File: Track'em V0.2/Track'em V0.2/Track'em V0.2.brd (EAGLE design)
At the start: 47.2 x 17 mm, 36 parts, among them IC1 SAM-M8Q, J1 CORTEX_DEBUG_PTH, U2 3.3V/150mA, Y1 26MHz

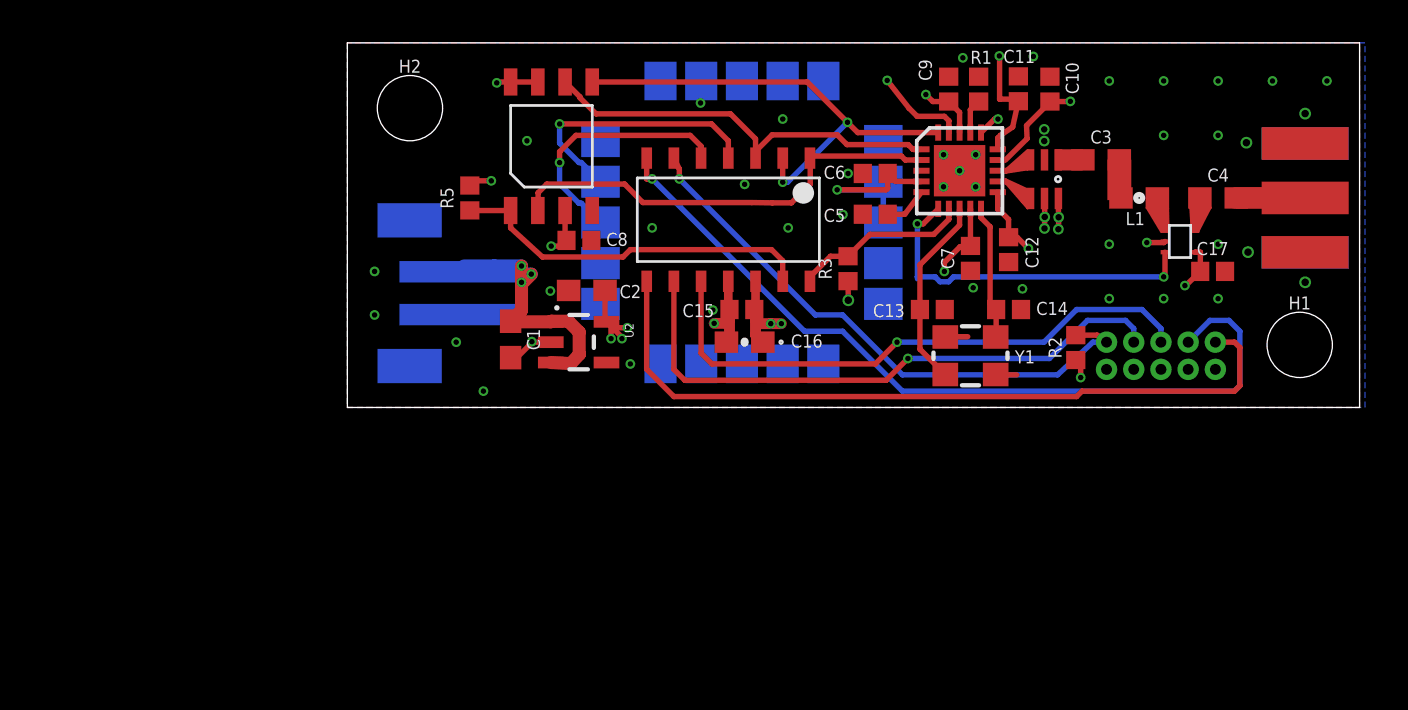
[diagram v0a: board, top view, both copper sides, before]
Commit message: tracking message parsed from GPS
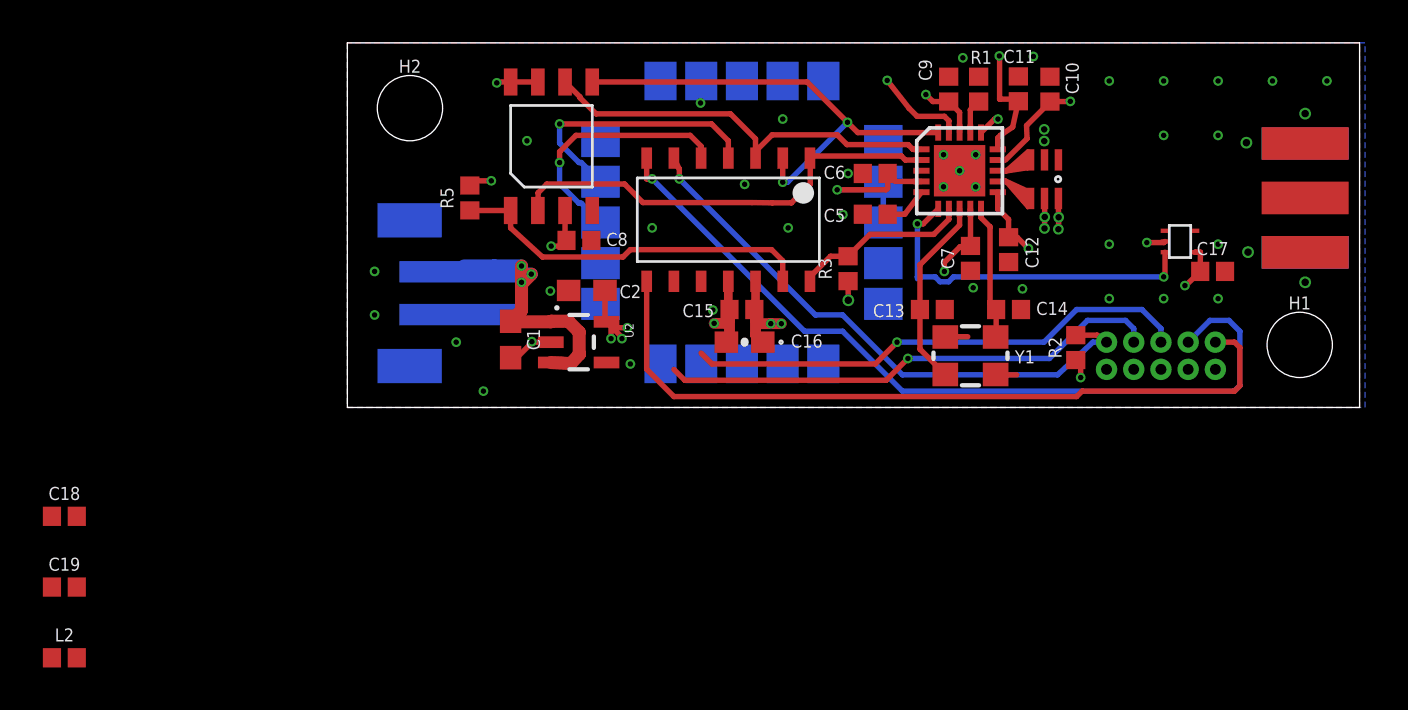
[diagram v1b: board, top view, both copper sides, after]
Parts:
- removed C3, C4: 1000pF, SparkFun-Capacitors:0603
- removed L1: 6.8nH, SparkFun-Passives:0603
- added C18, C19: 1000pF, SparkFun-Capacitors:0402
- added L2: 6.8NH, SparkFun-Coils:0402
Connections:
- net N$1: now also L2.2; no longer L1.2
- net N$13: now also C19.2; no longer C4.2
- net N$2: now also C18.2, L2.1; no longer C3.2, L1.1
- net N$3: now also C19.1; no longer C4.1
- net UBAL: now also C18.1; no longer C3.1
- net USART_RX: now also U$2.9; no longer U$2.10
- net USART_TX: now also U$2.10; no longer U$2.9
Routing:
- net N$1: track 10.5 -> 0.00 mm
- net N$3: track 9.14 -> 0.00 mm
- net USART_TX: track 27.7 -> 23.6 mm
- net USART_RX: track 27.1 -> 23.7 mm
- net N$13: track 3.21 -> 0.00 mm
- net N$2: track 1.81 -> 0.00 mm
- net UBAL: track 1.15 -> 0.00 mm
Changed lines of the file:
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@@
 <wire x1="47.244" y1="17.018" x2="0" y2="17.018" width="0" layer="20"/>
 <wire x1="0" y1="17.018" x2="0" y2="0" width="0" layer="20"/>
-<rectangle x1="33.0073" y1="11.0617" x2="34.3281" y2="12.0523" layer="1"/>
-<rectangle x1="35.4711" y1="9.6774" x2="36.5887" y2="11.5697" layer="1"/>
 <rectangle x1="33.02" y1="11.049" x2="36.7538" y2="12.0396" layer="39"/>
 <polygon width="0.508" layer="41">
@@
 <element name="J$1" library="SparkFun-Connectors" package="SMA-EDGE" value="SMA_EDGE" x="44.704" y="12.319" rot="R270"/>
 <element name="U$4" library="SaL-lib1" package="AN26018A" value="AN26018A" x="38.862" y="7.747" rot="R270"/>
-<element name="C3" library="SparkFun-Capacitors" package="0603" value="1000pF" x="35.179" y="11.557" smashed="yes">
-<attribute name="NAME" x="35.179" y="12.319" size="0.6096" layer="25" font="vector" ratio="20" align="bottom-center"/>
-<attribute name="PROD_ID" value="CAP-07888" x="35.179" y="11.557" size="1.778" layer="27" display="off"/>
-</element>
-<element name="L1" library="SparkFun-Passives" package="0603" value="6.8nH" x="36.957" y="9.779" smashed="yes">
-<attribute name="NAME" x="36.322" y="8.509" size="0.6096" layer="25" font="vector" ratio="20"/>
-</element>
-<element name="C4" library="SparkFun-Capacitors" package="0603" value="1000pF" x="40.64" y="9.779" smashed="yes">
-<attribute name="NAME" x="40.64" y="10.541" size="0.6096" layer="25" font="vector" ratio="20" align="bottom-center"/>
-<attribute name="PROD_ID" value="CAP-07888" x="40.64" y="9.779" size="1.778" layer="27" display="off"/>
-</element>
 <element name="H1" library="SparkFun-Hardware" package="STAND-OFF-TIGHT" value="STAND-OFFTIGHT" x="44.45" y="2.921" smashed="yes">
 <attribute name="NAME" x="44.45" y="4.572" size="0.6096" layer="25" font="vector" ratio="20" align="bottom-center"/>
@@
 <element name="C17" library="SparkFun-Capacitors" package="0402" value="0.1uF" x="40.386" y="6.35">
 <attribute name="PROD_ID" value="CAP-12416" x="40.386" y="6.35" size="1.778" layer="27" display="off"/>
+</element>
+<element name="C18" library="SparkFun-Capacitors" package="0402" value="1000pF" x="-13.208" y="-5.08">
+<attribute name="PROD_ID" value="CAP-12416" x="-13.208" y="-5.08" size="1.778" layer="27" display="off"/>
+</element>
+<element name="C19" library="SparkFun-Capacitors" package="0402" value="1000pF" x="-13.208" y="-8.382">
+<attribute name="PROD_ID" value="CAP-12416" x="-13.208" y="-8.382" size="1.778" layer="27" display="off"/>
+</element>
+<element name="L2" library="SparkFun-Coils" library_urn="urn:adsk.eagle:library:512" package="0402" package3d_urn="urn:adsk.eagle:package:37575/1" value="6.8NH" x="-13.208" y="-11.684">
+<attribute name="PROD_ID" value="NDUC-13457" x="-13.208" y="-11.684" size="1.778" layer="27" display="off"/>
 </element>
 </elements>
@@
 <signal name="N$13">
 <contactref element="J$1" pad="SIG"/>
-<contactref element="C4" pad="2"/>
-<wire x1="41.49" y1="9.779" x2="44.704" y2="9.779" width="1.016" layer="1"/>
+<contactref element="C19" pad="2"/>
+<wire x1="-12.628" y1="-8.382" x2="44.704" y2="9.779" width="0" layer="19" extent="1-1"/>
 </signal>
 <signal name="N$1">
 <contactref element="U$4" pad="1"/>
-<contactref element="L1" pad="2"/>
-<wire x1="37.9984" y1="8.2042" x2="37.3253" y2="9.3218" width="0.127" layer="1"/>
-<wire x1="37.3253" y1="9.3218" x2="37.336996875" y2="9.321646875" width="0.127" layer="1"/>
-<wire x1="37.336996875" y1="9.321646875" x2="38.2905" y2="9.3091" width="0.127" layer="1"/>
-<wire x1="38.2905" y1="9.3091" x2="38.3159" y2="8.2042" width="0.127" layer="1"/>
-<wire x1="38.3159" y1="8.2042" x2="38.2143" y2="9.2329" width="0.127" layer="1"/>
-<wire x1="38.2143" y1="9.2329" x2="37.4777" y2="9.2075" width="0.127" layer="1"/>
-<wire x1="37.4777" y1="9.2075" x2="38.0365" y2="8.3693" width="0.127" layer="1"/>
-<wire x1="38.0365" y1="8.3693" x2="38.2016" y2="8.382" width="0.127" layer="1"/>
-<wire x1="38.2016" y1="8.382" x2="38.1127" y2="9.144" width="0.127" layer="1"/>
-<wire x1="38.1127" y1="9.144" x2="37.6301" y2="9.1186" width="0.127" layer="1"/>
-<wire x1="37.6301" y1="9.1186" x2="38.0873" y2="8.4709" width="0.127" layer="1"/>
-<wire x1="38.0873" y1="8.4709" x2="38.0111" y2="9.0424" width="0.127" layer="1"/>
-<wire x1="38.0111" y1="9.0424" x2="37.7825" y2="9.0424" width="0.127" layer="1"/>
-<wire x1="37.7825" y1="9.0424" x2="37.973" y2="8.7757" width="0.127" layer="1"/>
-<wire x1="37.973" y1="8.7757" x2="37.9095" y2="8.9662" width="0.127" layer="1"/>
-<wire x1="38.162" y1="8.247" x2="38.162" y2="8.3424" width="0.127" layer="1"/>
-<wire x1="38.162" y1="8.3424" x2="38.2016" y2="8.382" width="0.127" layer="1"/>
-<wire x1="37.807" y1="9.779" x2="37.349646875" y2="9.321646875" width="0.127" layer="1"/>
-<wire x1="37.349646875" y1="9.321646875" x2="37.336996875" y2="9.321646875" width="0.127" layer="1"/>
-</signal>
-<signal name="N$2">
-<contactref element="L1" pad="1"/>
-<contactref element="C3" pad="2"/>
-<wire x1="36.107" y1="9.779" x2="36.107" y2="11.479" width="0.254" layer="1"/>
-<wire x1="36.107" y1="11.479" x2="36.029" y2="11.557" width="0.254" layer="1"/>
+<contactref element="L2" pad="2"/>
+<wire x1="-12.628" y1="-11.684" x2="38.162" y2="8.247" width="0" layer="19" extent="1-1"/>
 </signal>
 <signal name="N$3">
 <contactref element="U$4" pad="5"/>
-<contactref element="C4" pad="1"/>
-<wire x1="39.3573" y1="9.3345" x2="39.4208" y2="8.2169" width="0.127" layer="1"/>
-<wire x1="39.4208" y1="8.2169" x2="39.7002" y2="8.2169" width="0.127" layer="1"/>
-<wire x1="39.7002" y1="8.2169" x2="40.2717" y2="9.3218" width="0.127" layer="1"/>
-<wire x1="40.2717" y1="9.3218" x2="39.4462" y2="9.2456" width="0.127" layer="1"/>
-<wire x1="39.4462" y1="9.2456" x2="39.5351" y2="8.3693" width="0.127" layer="1"/>
-<wire x1="39.5351" y1="8.3693" x2="39.6748" y2="8.3947" width="0.127" layer="1"/>
-<wire x1="39.6748" y1="8.3947" x2="40.1193" y2="9.2202" width="0.127" layer="1"/>
-<wire x1="40.1193" y1="9.2202" x2="39.5478" y2="9.144" width="0.127" layer="1"/>
-<wire x1="39.5478" y1="9.144" x2="39.624" y2="8.4836" width="0.127" layer="1"/>
-<wire x1="39.624" y1="8.4836" x2="39.9669" y2="9.1186" width="0.127" layer="1"/>
-<wire x1="39.9669" y1="9.1186" x2="39.6621" y2="9.0678" width="0.127" layer="1"/>
-<wire x1="39.6621" y1="9.0678" x2="39.6748" y2="8.7503" width="0.127" layer="1"/>
-<wire x1="39.6748" y1="8.7503" x2="39.8018" y2="9.017" width="0.127" layer="1"/>
-<wire x1="39.562" y1="8.247" x2="39.562" y2="8.2819" width="0.127" layer="1"/>
-<wire x1="39.562" y1="8.2819" x2="39.6748" y2="8.3947" width="0.127" layer="1"/>
-<wire x1="39.79" y1="9.779" x2="39.3573" y2="9.3463" width="0.127" layer="1"/>
-<wire x1="39.3573" y1="9.3463" x2="39.3573" y2="9.3345" width="0.127" layer="1"/>
+<contactref element="C19" pad="1"/>
+<wire x1="-13.788" y1="-8.382" x2="39.562" y2="8.247" width="0" layer="19" extent="1-1"/>
 </signal>
 <signal name="UBAL">
-<contactref element="C3" pad="1"/>
 <contactref element="U$3" pad="1"/>
-<wire x1="33.1874" y1="11.5553" x2="34.318" y2="11.568" width="0.254" layer="1"/>
-<wire x1="34.318" y1="11.568" x2="34.329" y2="11.557" width="0.254" layer="1"/>
+<wire x1="33.1874" y1="11.5553" x2="34.318" y2="11.568" width="0" layer="19" extent="1-16"/>
+<contactref element="C18" pad="1"/>
+<wire x1="-13.788" y1="-5.08" x2="33.1874" y2="11.5553" width="0" layer="19" extent="1-1"/>
 </signal>
 <signal name="RF_N">
@@
 <signal name="USART_RX">
 <contactref element="J1" pad="6"/>
-<contactref element="U$2" pad="10"/>
 <wire x1="37.973" y1="3.048" x2="37.973" y2="3.683" width="0.254" layer="16"/>
 <wire x1="37.973" y1="3.683" x2="37.084" y2="4.572" width="0.254" layer="16"/>
 <wire x1="37.084" y1="4.572" x2="34.036" y2="4.572" width="0.254" layer="16"/>
 <wire x1="32.512" y1="3.048" x2="34.036" y2="4.572" width="0.254" layer="16"/>
-<wire x1="16.51" y1="5.888" x2="16.51" y2="2.54" width="0.254" layer="1"/>
 <wire x1="16.51" y1="2.54" x2="17.018" y2="2.032" width="0.254" layer="1"/>
 <wire x1="24.638" y1="2.032" x2="25.654" y2="3.048" width="0.254" layer="1"/>
@@
 <wire x1="17.018" y1="2.032" x2="24.638" y2="2.032" width="0.254" layer="1"/>
 <wire x1="25.654" y1="3.048" x2="32.512" y2="3.048" width="0.254" layer="16"/>
+<contactref element="U$2" pad="9"/>
+<wire x1="16.51" y1="2.54" x2="15.24" y2="5.888" width="0" layer="19" extent="1-1"/>
 </signal>
 <signal name="USART_TX">
 <contactref element="J1" pad="8"/>
-<contactref element="U$2" pad="9"/>
 <wire x1="36.703" y1="3.048" x2="36.703" y2="3.683" width="0.254" layer="16"/>
 <wire x1="36.322" y1="4.064" x2="34.544" y2="4.064" width="0.254" layer="16"/>
 <wire x1="32.766" y1="2.286" x2="34.544" y2="4.064" width="0.254" layer="16"/>
 <wire x1="36.703" y1="3.683" x2="36.322" y2="4.064" width="0.254" layer="16"/>
-<wire x1="15.24" y1="5.888" x2="15.24" y2="1.778" width="0.254" layer="1"/>
 <wire x1="15.24" y1="1.778" x2="15.748" y2="1.27" width="0.254" layer="1"/>
 <wire x1="25.146" y1="1.27" x2="26.162" y2="2.286" width="0.254" layer="1"/>
@@
 <wire x1="15.748" y1="1.27" x2="25.146" y2="1.27" width="0.254" layer="1"/>
 <wire x1="26.162" y1="2.286" x2="32.766" y2="2.286" width="0.254" layer="16"/>
+<contactref element="U$2" pad="10"/>
+<wire x1="15.24" y1="1.778" x2="16.51" y2="5.888" width="0" layer="19" extent="1-1"/>
 </signal>
 <signal name="RAW">
@@
 <wire x1="28.575" y1="8.509" x2="26.725" y2="6.659" width="0.254" layer="1"/>
 </signal>
+<signal name="N$2">
+<contactref element="L2" pad="1"/>
+<contactref element="C18" pad="2"/>
+<wire x1="-12.628" y1="-5.08" x2="-13.788" y2="-11.684" width="0" layer="19" extent="1-1"/>
+</signal>
 </signals>

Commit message: setting up trackem v0.2
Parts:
- removed C18: 1000pF, SparkFun-Capacitors:0402
- removed U$3: 0433BM15A0001, SaL-lib1:0433BM15A0001
- removed U$4: AN26018A, SaL-lib1:AN26018A
- added C20, C21: 1000pF, SparkFun-Capacitors:0402
- added C3: 3.9pF, SparkFun-Capacitors:0402
- added C4: 8.2pF, SparkFun-Capacitors:0402
- added L1, L3: 27NH, SparkFun-Coils:0402
- added L4: 6.8NH, SparkFun-Coils:0402
- C17: value 0.1uF -> 220pF
- moved L2 52.4 mm to (35.3, 8.13)
- moved C19 50.2 mm to (34.8, 6.35), turned to 270 degrees
- moved C17 7.37 mm to (33.0, 6.10), turned to 270 degrees
- moved C10 0.98 mm to (31.8, 14.8)
- moved C11 0.72 mm to (30.6, 14.8)
- moved C9 0.21 mm to (27.9, 14.9)
- moved R1 0.15 mm to (29.3, 14.9)
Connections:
- removed net N$13: C19.2, J$1.SIG
- removed net UBAL: C18.1, U$3.1
- new net ANT: C21.2, J$1.SIG
- new net N$5: C20.1, C21.1, L2.2
- net 3.3V: no longer C17.1, U$4.4
- net CNT: no longer U$4.3
- net GND: now also C3.2; no longer U$3.2, U$3.5, U$3.6, U$4.2
- net N$1: now also C17.1, L1.1; no longer L2.2, U$4.1
- net N$2: now also C4.1, L3.2, L4.1; no longer C18.2, L2.1
- net N$3: now also L2.1, L4.2; no longer U$4.5
- net RF_N: now also C3.1, L3.1; no longer U$3.3
- net RF_P: now also C4.2, L1.2; no longer U$3.4
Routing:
- net CNT: track 16.7 -> 0.00 mm, vias 2 -> 0
- net 3.3V: track 49.5 -> 38.8 mm, vias 18 -> 15
- net RF_P: track 8.53 -> 0.00 mm
- net RF_N: track 7.70 -> 0.00 mm
- net GND: track 17.0 -> 13.0 mm, vias 45 -> 22
